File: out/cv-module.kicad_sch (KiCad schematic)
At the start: 189 parts, among them J1 CH1, J10 CTRL2, J11 CTRL3, J2 CH2, J3 CH3, J4 CH4, J5 CH5, J6 CH6, J7 BOND, J8 PWR, J9 CTRL, K101 DPDT latch, K102 DPDT latch, K201 DPDT latch, K202 DPDT latch, K301 DPDT latch, K302 DPDT latch, K401 DPDT latch, K402 DPDT latch, K501 DPDT latch, K502 DPDT latch, K601 DPDT latch, K602 DPDT latch, U1 OPA1644, U10 SSI2164, U11 74AHC541, U12 MAX6126A25, U2 OPA1644, U3 OPA1644, U4 OPA1644, U5 OPA1644, U6 OPA1644, U7 OPA1644, U8 OPA1644, U9 SSI2164

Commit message: Moved md files to docs and no longer have any depedendencies on code in the sibling mixer project
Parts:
- added unit 4 of U8
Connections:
- net AGND: now also R901.2; no longer R901.1
- net IOUT1: no longer C131.2, R132.1, U5.1
- net IOUT2: no longer C231.2, R232.1, U5.7
- net IOUT3: no longer C331.2, R332.1, U5.8
- net IOUT4: no longer C431.2, R432.1, U5.14
- net IOUT5: no longer C531.2, R532.1, U6.1
- net IOUT6: no longer C631.2, R632.1, U6.7
- net MAGND: now also R901.1, R902.1, U8.12 (+); no longer C131.1, C142.1, C231.1, C242.1, C331.1, C342.1, C431.1, C442.1, C531.1, C542.1, C631.1, C642.1, R131.2, R143.2, R231.2, R243.2, R331.2, R343.2, R431.2, R443.2, R531.2, R543.2, R631.2, R643.2, R801.2, R802.1, R901.2, R902.2, U5.13 (-), U5.2 (-), U5.6 (-), U5.9 (-), U6.2 (-), U6.6 (-), U7.13 (-), U7.2 (-), U7.6 (-), U7.9 (-), U8.2 (-), U8.6 (-), U8.9 (-)
- net MDGND: now also R902.2; no longer K101.A2, K101.B2, K102.A2, K102.B2, K201.A2, K201.B2, K202.A2, K202.B2, K301.A2, K301.B2, K302.A2, K302.B2, K401.A2, K401.B2, K402.A2, K402.B2, K501.A2, K501.B2, K502.A2, K502.B2, K601.A2, K601.B2, K602.A2, K602.B2, R902.1
- net RCJ3: now reaches C302.1, R315.2
- net FEN5: now reaches R501.2, R502.1, U2.2 (-)
- net CVX1: now reaches C141.1, R141.2, R142.1, R143.1, R144.2
- net CVX6: now reaches C641.1, R641.2, R642.1, R643.1, R644.2
- net RCJ2: now reaches C202.1, R215.2
- net CVX3: now reaches C341.1, R341.2, R342.1, R343.1, R344.2
- net CVX4: now reaches C441.1, R441.2, R442.1, R443.1, R444.2
- net RCJ5: now reaches C502.1, R515.2
- net FEN6: now reaches R601.2, R602.1, U2.6 (-)
- net CVX2: now reaches C241.1, R241.2, R242.1, R243.1, R244.2
- net RCJ6: now reaches C602.1, R615.2
- net RCJ4: now reaches C402.1, R415.2
- net FEN2: now reaches R201.2, R202.1, U1.6 (-)
- net RCJ1: now reaches C102.1, R115.2
- net CVX5: now reaches C541.1, R541.2, R542.1, R543.1, R544.2
- net FEN1: now reaches R101.2, R102.1, U1.2 (-)
- net FEN3: now reaches R301.2, R302.1, U1.9 (-)
- net FEN4: now reaches R401.2, R402.1, U1.13 (-)
- net KK101R: no longer names the net of K101.B1
- net KK101S: no longer names the net of K101.A1
- net KK102R: no longer names the net of K102.B1
- net KK102S: no longer names the net of K102.A1
- net KK201R: no longer names the net of K201.B1
- net KK201S: no longer names the net of K201.A1
- net KK202R: no longer names the net of K202.B1
- net KK202S: no longer names the net of K202.A1
- net KK301R: no longer names the net of K301.B1
- net KK301S: no longer names the net of K301.A1
- net KK302R: no longer names the net of K302.B1
- net KK302S: no longer names the net of K302.A1
- net KK401R: no longer names the net of K401.B1
- net KK401S: no longer names the net of K401.A1
- net KK402R: no longer names the net of K402.B1
- net KK402S: no longer names the net of K402.A1
- net KK501R: no longer names the net of K501.B1
- net KK501S: no longer names the net of K501.A1
- net KK502R: no longer names the net of K502.B1
- net KK502S: no longer names the net of K502.A1
- net KK601R: no longer names the net of K601.B1
- net KK601S: no longer names the net of K601.A1
- net KK602R: no longer names the net of K602.B1
- net KK602S: no longer names the net of K602.A1
- new net CVN1: C142.1, R143.2, U7.2 (-)
- new net CVN2: C242.1, R243.2, U7.6 (-)
- new net CVN3: C342.1, R343.2, U7.9 (-)
- new net CVN4: C442.1, R443.2, U7.13 (-)
- new net CVN5: C542.1, R543.2, U8.2 (-)
- new net CVN6: C642.1, R643.2, U8.6 (-)
- new net RINV: R801.2, R802.1, U8.9 (-)
- new net SPARE: U8.13 (-), U8.14
- new net SRV1: C131.2, R132.1, U5.1
- new net SRV2: C231.2, R232.1, U5.7
- new net SRV3: C331.2, R332.1, U5.8
- new net SRV4: C431.2, R432.1, U5.14
- new net SRV5: C531.2, R532.1, U6.1
- new net SRV6: C631.2, R632.1, U6.7
- new net SVN1: C131.1, R131.2, U5.2 (-)
- new net SVN2: C231.1, R231.2, U5.6 (-)
- new net SVN3: C331.1, R331.2, U5.9 (-)
- new net SVN4: C431.1, R431.2, U5.13 (-)
- new net SVN5: C531.1, R531.2, U6.2 (-)
- new net SVN6: C631.1, R631.2, U6.6 (-)
- no-connect marks 24 -> 74
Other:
- moved on the sheet: R132, R232, R332, R432, R532, R632, R801, R901, R902

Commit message: tidy up
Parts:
- removed C804: 10u/16V X7R, Capacitor_SMD:C_1210_3225Metric, symbol Device:C

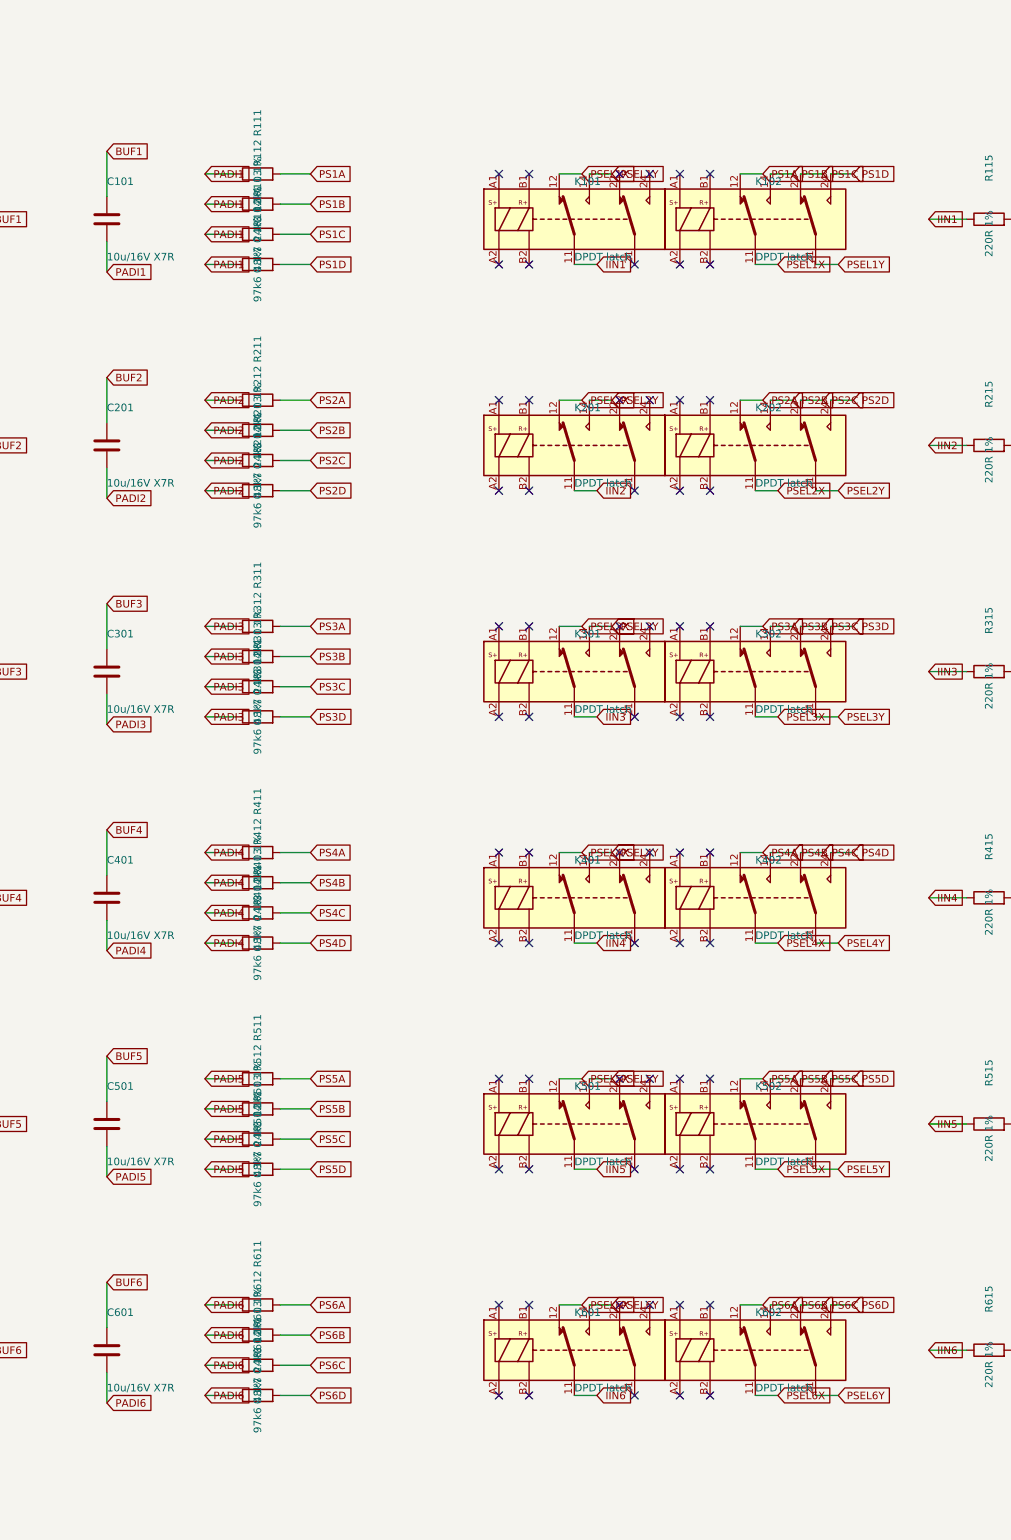
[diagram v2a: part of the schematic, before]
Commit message: TASK — is the 2-bit coarse pad worth 52% of the board?
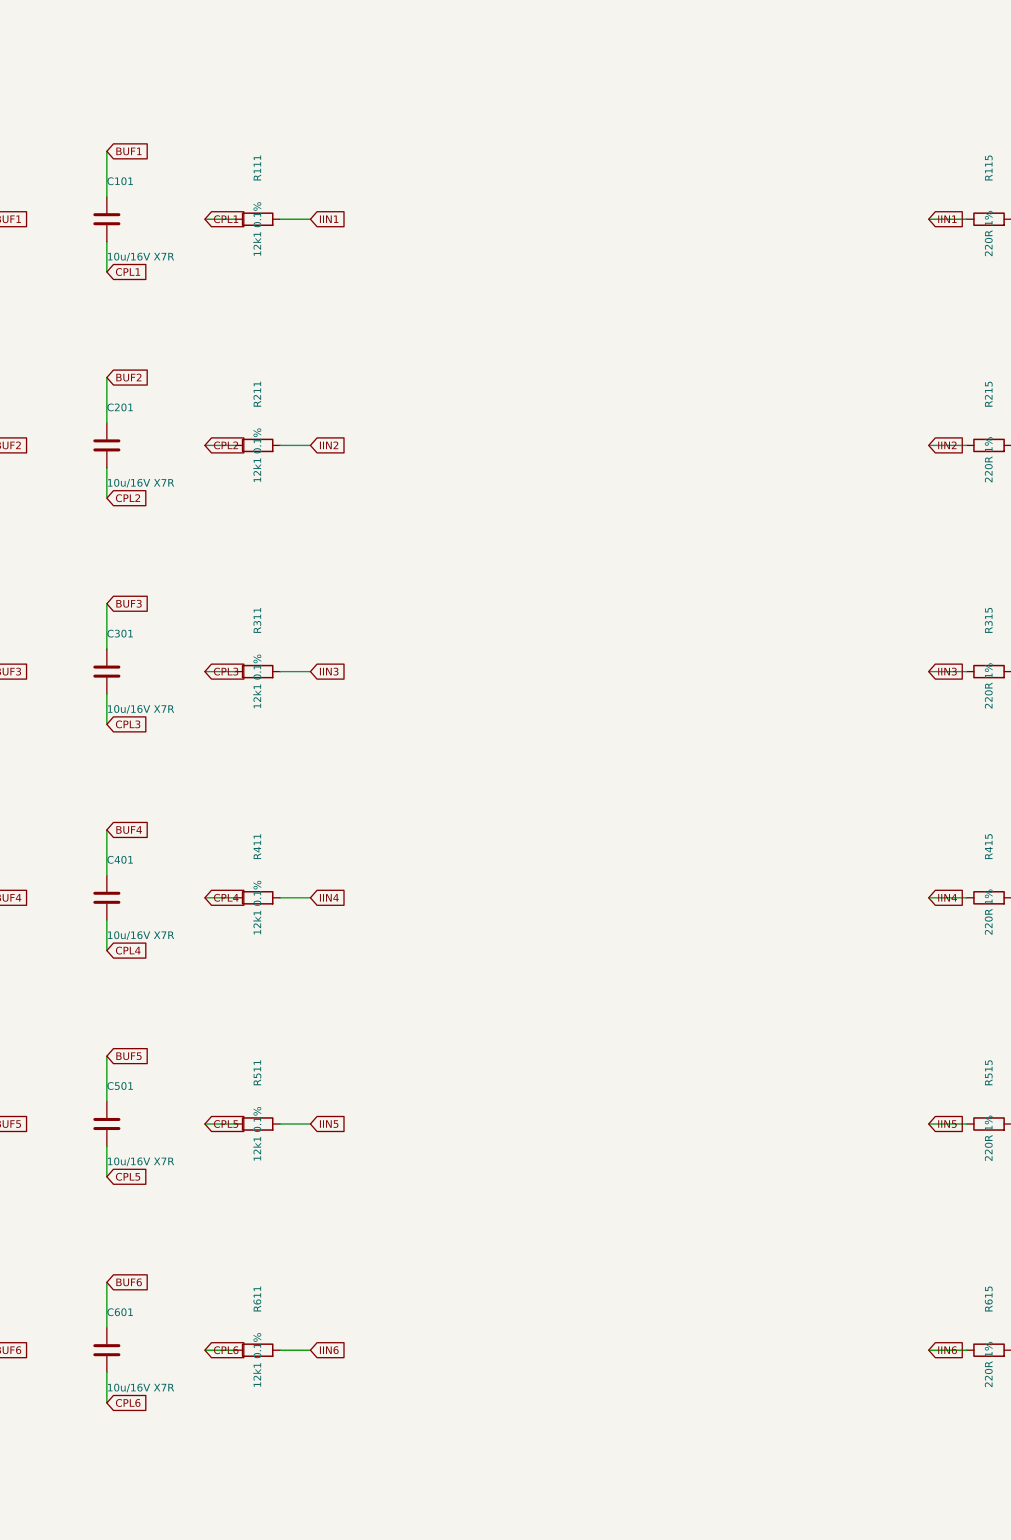
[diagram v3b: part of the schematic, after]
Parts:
- removed K101, K102, K201, K202, K301, K302, K401, K402, K501, K502, K601, K602: DPDT latch, symbol cv:Relay
- removed R112, R212, R312, R412, R512, R612: 24k3 0.1%, Resistor_SMD:R_0805_2012Metric, symbol Device:R
- removed R113, R213, R313, R413, R513, R613: 48k7 0.1%, Resistor_SMD:R_0805_2012Metric, symbol Device:R
- removed R114, R214, R314, R414, R514, R614: 97k6 0.1%, Resistor_SMD:R_0805_2012Metric, symbol Device:R
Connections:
- net PS1A is gone; now on net IIN1: R111.2
- net PS2A is gone; now on net IIN2: R211.2
- net PS3A is gone; now on net IIN3: R311.2
- net PS4A is gone; now on net IIN4: R411.2
- net PS5A is gone; now on net IIN5: R511.2
- net PS6A is gone; now on net IIN6: R611.2
- net PADI1 renamed CPL1
- net PADI2 renamed CPL2
- net PADI3 renamed CPL3
- net PADI4 renamed CPL4
- net PADI5 renamed CPL5
- net PADI6 renamed CPL6
- no-connect marks 74 -> 8
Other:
- moved on the sheet: R111, R211, R311, R411, R511, R611

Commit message: envelope rectifier and fail-safe
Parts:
- added C151, C251, C351, C451, C551, C651: 470n/50V X7R, Capacitor_SMD:C_0805_2012Metric, symbol Device:C
- added C721, C722, C723, C724: 100n/50V X7R, Capacitor_SMD:C_0805_2012Metric, symbol Device:C
- added C805: 2n2/50V C0G, Capacitor_SMD:C_0805_2012Metric, symbol Device:C
- added C806: 1u/16V X7R, Capacitor_SMD:C_0805_2012Metric, symbol Device:C
- added D151, D152, D251, D252, D351, D352, D451, D452, D551, D552, D651, D652: 1N4148W, Diode_SMD:D_SOD-123, symbol Device:D
- added D801, D802, D803, D813, D823, D833: BAT54, Diode_SMD:D_SOD-123, symbol Device:D
- added K801, K802, K803: DPDT, symbol cv:Relay
- added Q801: None, Package_TO_SOT_SMD:SOT-23, symbol cv:Q_NMOS_GSD
- added R151, R152, R153, R155, R251, R252, R253, R255, R351, R352, R353, R355, R451, R452, R453, R455, R551, R552, R553, R555, R651, R652, R653, R655: 10k 1%, Resistor_SMD:R_0805_2012Metric, symbol Device:R
- added R154, R254, R354, R454, R554, R654: 4k99 1%, Resistor_SMD:R_0805_2012Metric, symbol Device:R
- added R803: 100k 1%, Resistor_SMD:R_0805_2012Metric, symbol Device:R
- added U13, U14: TL074, Package_SO:SOIC-14_3.9x8.7mm_P1.27mm, symbol cv:TL074
- added unit 4 of U2
- added unit 3 of U2
- added unit 4 of U4
- added unit 3 of U4
- added unit 4 of U6
- added unit 3 of U6
- J11: footprint Connector_PinHeader_2.54mm:PinHeader_1x03_P2.54mm_Vertical -> Connector_PinHeader_2.54mm:PinHeader_1x05_P2.54mm_Vertical; symbol Connector_Generic:Conn_01x03 -> Connector_Generic:Conn_01x05
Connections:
- net BUF1: now also R151.1, R153.1
- net BUF2: now also R251.1, R253.1
- net BUF3: now also R351.1, R353.1
- net BUF4: now also R451.1, R453.1
- net BUF5: now also R551.1, R553.1
- net BUF6: now also R651.1, R653.1
- net MAGND: now also C721.2, C722.2, C723.2, C724.2, D803.1 (K), U13.10 (+), U13.12 (+), U13.3 (+), U13.5 (+), U14.10 (+), U14.12 (+), U14.3 (+), U14.5 (+), U2.10 (+), U2.12 (+), U4.10 (+), U4.12 (+), U6.10 (+), U6.12 (+)
- net MDGND: now also J11.4 (Pin_4), C806.2, D801.2 (A), Q801.2 (S), R803.2
- net PIN1: now also K801.12
- net PIN2: now also K801.22
- net PIN3: now also K802.12
- net PIN4: now also K802.22
- net PIN5: now also K803.12
- net PIN6: now also K803.22
- net SIN1: now also K801.11; no longer C121.2, R121.2, R131.1, U3.1
- net SIN2: now also K801.21; no longer C221.2, R221.2, R231.1, U3.7
- net SIN3: now also K802.11; no longer C321.2, R321.2, R331.1, U3.8
- net SIN4: now also K802.21; no longer C421.2, R421.2, R431.1, U3.14
- net SIN5: now also K803.11; no longer C521.2, R521.2, R531.1, U4.1
- net SIN6: now also K803.21; no longer C621.2, R621.2, R631.1, U4.7
- net V5: now also D813.1 (K), D823.1 (K), D833.1 (K), K801.A1, K802.A1, K803.A1
- net VA+: now also C721.1, C723.1, U13.4 (V+), U14.4 (V+)
- net VA-: now also C722.1, C724.1, U13.11 (V-), U14.11 (V-)
- net VREFN: now also D803.2 (A)
- net SPARE renamed SPARE0
- new net AOUT1: D151.2 (A), D152.1 (K), U13.1
- new net AOUT2: D251.2 (A), D252.1 (K), U13.7
- new net AOUT3: D351.2 (A), D352.1 (K), U13.8
- new net AOUT4: D451.2 (A), D452.1 (K), U13.14
- new net AOUT5: D551.2 (A), D552.1 (K), U14.1
- new net AOUT6: D651.2 (A), D652.1 (K), U14.7
- new net ENV1: C151.2, R155.2, U2.8
- new net ENV2: C251.2, R255.2, U2.14
- new net ENV3: C351.2, R355.2, U4.8
- new net ENV4: C451.2, R455.2, U4.14
- new net ENV5: C551.2, R555.2, U6.8
- new net ENV6: C651.2, R655.2, U6.14
- new net ENVN1: C151.1, R153.2, R154.2, R155.1, U2.9 (-)
- new net ENVN2: C251.1, R253.2, R254.2, R255.1, U2.13 (-)
- new net ENVN3: C351.1, R353.2, R354.2, R355.1, U4.9 (-)
- new net ENVN4: C451.1, R453.2, R454.2, R455.1, U4.13 (-)
- new net ENVN5: C551.1, R553.2, R554.2, R555.1, U6.9 (-)
- new net ENVN6: C651.1, R653.2, R654.2, R655.1, U6.13 (-)
- new net FSAC: C805.2, D801.1 (K), D802.2 (A)
- new net FSD: D813.2 (A), D823.2 (A), D833.2 (A), K801.A2, K802.A2, K803.A2, Q801.3 (D)
- new net FSDRV: C805.1, J11.5 (Pin_5)
- new net FSG: C806.1, D802.1 (K), Q801.1 (G), R803.1
- new net HW1: D152.2 (A), R152.2, R154.1
- new net HW2: D252.2 (A), R252.2, R254.1
- new net HW3: D352.2 (A), R352.2, R354.1
- new net HW4: D452.2 (A), R452.2, R454.1
- new net HW5: D552.2 (A), R552.2, R554.1
- new net HW6: D652.2 (A), R652.2, R654.1
- new net HWN1: D151.1 (K), R151.2, R152.1, U13.2 (-)
- new net HWN2: D251.1 (K), R251.2, R252.1, U13.6 (-)
- new net HWN3: D351.1 (K), R351.2, R352.1, U13.9 (-)
- new net HWN4: D451.1 (K), R451.2, R452.1, U13.13 (-)
- new net HWN5: D551.1 (K), R551.2, R552.1, U14.2 (-)
- new net HWN6: D651.1 (K), R651.2, R652.1, U14.6 (-)
- new net IVOUT1: C121.2, K801.14, R121.2, R131.1, U3.1
- new net IVOUT2: C221.2, K801.24, R221.2, R231.1, U3.7
- new net IVOUT3: C321.2, K802.14, R321.2, R331.1, U3.8
- new net IVOUT4: C421.2, K802.24, R421.2, R431.1, U3.14
- new net IVOUT5: C521.2, K803.14, R521.2, R531.1, U4.1
- new net IVOUT6: C621.2, K803.24, R621.2, R631.1, U4.7
- new net SPARE1: U14.8, U14.9 (-)
- new net SPARE2: U14.13 (-), U14.14
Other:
- note added: "Fail-safe: any stuck MCU state collapses the pump, the FET releases, and de-energised is bypass. D803 covers the one path the pump cannot see. See design.fail_safe()."
- moved on the sheet: C701, C702, C703, C704, C705, C706, C707, C708, C709, C710, C711, C712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

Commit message: Next increment
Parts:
- D803: value BAT54 -> PMEG2010AEH; footprint Diode_SMD:D_SOD-123 -> Diode_SMD:D_SOD-123F
- Q801: value None -> DMG1012T; footprint Package_TO_SOT_SMD:SOT-23 -> Package_TO_SOT_SMD:SOT-523
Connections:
- net FSD: now also K801.12, K802.12, K803.12; no longer K801.A2, K802.A2, K803.A2
- net IVOUT1: now also K801.8; no longer K801.14
- net IVOUT2: now also K801.5; no longer K801.24
- net IVOUT3: now also K802.8; no longer K802.14
- net IVOUT4: now also K802.5; no longer K802.24
- net IVOUT5: now also K803.8; no longer K803.14
- net IVOUT6: now also K803.5; no longer K803.24
- net PIN1: now also K801.10; no longer K801.12
- net PIN2: now also K801.3; no longer K801.22
- net PIN3: now also K802.10; no longer K802.12
- net PIN4: now also K802.3; no longer K802.22
- net PIN5: now also K803.10; no longer K803.12
- net PIN6: now also K803.3; no longer K803.22
- net SIN1: now also K801.9; no longer K801.11
- net SIN2: now also K801.4; no longer K801.21
- net SIN3: now also K802.9; no longer K802.11
- net SIN4: now also K802.4; no longer K802.21
- net SIN5: now also K803.9; no longer K803.11
- net SIN6: now also K803.4; no longer K803.21
- net V5: now also K801.1, K802.1, K803.1; no longer K801.A1, K802.A1, K803.A1
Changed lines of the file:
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@@
 		(pts
 			(xy 815.34 977.9)
-			(xy 815.34 965.2)
+			(xy 815.34 970.28)
 		)
 		(stroke
@@
 		(pts
 			(xy 820.42 977.9)
-			(xy 820.42 960.12)
+			(xy 820.42 970.28)
 		)
 		(stroke
@@
 		(pts
 			(xy 825.5 977.9)
-			(xy 825.5 955.04)
+			(xy 825.5 970.28)
 		)
 		(stroke
@@
 		(pts
 			(xy 866.14 977.9)
-			(xy 866.14 965.2)
+			(xy 866.14 970.28)
 		)
 		(stroke
@@
 		(pts
 			(xy 871.22 977.9)
-			(xy 871.22 960.12)
+			(xy 871.22 970.28)
 		)
 		(stroke
@@
 		(pts
 			(xy 876.3 977.9)
-			(xy 876.3 955.04)
+			(xy 876.3 970.28)
 		)
 		(stroke
@@
 		(pts
 			(xy 916.94 977.9)
-			(xy 916.94 965.2)
+			(xy 916.94 970.28)
 		)
 		(stroke
@@
 		(pts
 			(xy 922.02 977.9)
-			(xy 922.02 960.12)
+			(xy 922.02 970.28)
 		)
 		(stroke
@@
 		(pts
 			(xy 927.1 977.9)
-			(xy 927.1 955.04)
+			(xy 927.1 970.28)
 		)
 		(stroke
@@
 	(global_label "IVOUT1"
 		(shape input)
-		(at 815.34 965.2 0)
+		(at 815.34 970.28 0)
 		(effects
 			(font
@@
 	(global_label "PIN2"
 		(shape input)
-		(at 820.42 960.12 0)
+		(at 820.42 970.28 0)
 		(effects
 			(font
@@
 	(global_label "IVOUT2"
 		(shape input)
-		(at 825.5 955.04 0)
+		(at 825.5 970.28 0)
 		(effects
 			(font
@@
 	(global_label "IVOUT3"
 		(shape input)
-		(at 866.14 965.2 0)
+		(at 866.14 970.28 0)
 		(effects
 			(font
@@
 	(global_label "PIN4"
 		(shape input)
-		(at 871.22 960.12 0)
+		(at 871.22 970.28 0)
 		(effects
 			(font
@@
 	(global_label "IVOUT4"
 		(shape input)
-		(at 876.3 955.04 0)
+		(at 876.3 970.28 0)
 		(effects
 			(font
@@
 	(global_label "IVOUT5"
 		(shape input)
-		(at 916.94 965.2 0)
+		(at 916.94 970.28 0)
 		(effects
 			(font
@@
 	(global_label "PIN6"
 		(shape input)
-		(at 922.02 960.12 0)
+		(at 922.02 970.28 0)
 		(effects
 			(font
@@
 	(global_label "IVOUT6"
 		(shape input)
-		(at 927.1 955.04 0)
+		(at 927.1 970.28 0)
 		(effects
 			(font
@@
 			)
 		)
-		(property "Value" "None"
+		(property "Value" "DMG1012T"
 			(at 1016 946.15 0)
 			(effects
@@
 			)
 		)
-		(property "Footprint" "Package_TO_SOT_SMD:SOT-23"
+		(property "Footprint" "Package_TO_SOT_SMD:SOT-523"
 			(at 1016 939.8 0)
 			(effects
@@
 			)
 		)
-		(pin "11"
+		(pin "1"
 		)
-		(pin "12"
+		(pin "3"
 		)
-		(pin "14"
+		(pin "4"
 		)
-		(pin "21"
+		(pin "5"
 		)
-		(pin "22"
+		(pin "8"
 		)
-		(pin "24"
+		(pin "9"
 		)
-		(pin "A1"
+		(pin "10"
 		)
-		(pin "A2"
+		(pin "12"
 		)
 		(instances
@@
 			)
 		)
-		(pin "11"
+		(pin "1"
 		)
-		(pin "12"
+		(pin "3"
 		)
-		(pin "14"
+		(pin "4"
 		)
-		(pin "21"
+		(pin "5"
 		)
-		(pin "22"
+		(pin "8"
 		)
-		(pin "24"
+		(pin "9"
 		)
-		(pin "A1"
+		(pin "10"
 		)
-		(pin "A2"
+		(pin "12"
 		)
 		(instances
@@
 			)
 		)
-		(pin "11"
+		(pin "1"
 		)
-		(pin "12"
+		(pin "3"
 		)
-		(pin "14"
+		(pin "4"
 		)
-		(pin "21"
+		(pin "5"
 		)
-		(pin "22"
+		(pin "8"
 		)
-		(pin "24"
+		(pin "9"
 		)
-		(pin "A1"
+		(pin "10"
 		)
-		(pin "A2"
+		(pin "12"
 		)
 		(instances
@@
 			)
 		)
-		(property "Value" "BAT54"
+		(property "Value" "PMEG2010AEH"
 			(at 1092.2 946.15 0)
 			(effects
@@
 			)
 		)
-		(property "Footprint" "Diode_SMD:D_SOD-123"
+		(property "Footprint" "Diode_SMD:D_SOD-123F"
 			(at 1092.2 939.8 0)
 			(effects

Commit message: DC_DC power
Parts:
- added C807, C808, C811, C812, C813: 10u/50V X7R, Capacitor_SMD:C_1210_3225Metric, symbol Device:C
- added C809: 100n/50V X7R, Capacitor_SMD:C_0805_2012Metric, symbol Device:C
- added C810: 470n/50V X7R, Capacitor_SMD:C_0805_2012Metric, symbol Device:C
- added C814: 10u/16V X7R, Capacitor_SMD:C_1210_3225Metric, symbol Device:C
- added D804: B340A, Diode_SMD:D_SMA, symbol Device:D_Schottky
- added R804, R805: 4R7 1%, Resistor_SMD:R_0805_2012Metric, symbol Device:R
- added U15: TMR6-2422WI, cv:TRACO_TMR-6-xxxxWI_Dual_THT, symbol cv:TMR6-2422WI
- added U16: NCP1117-5.0, Package_TO_SOT_SMD:TO-252-2, symbol cv:NCP1117-5.0
- J8: footprint Connector_PinHeader_2.54mm:PinHeader_1x05_P2.54mm_Vertical -> Connector_PinHeader_2.54mm:PinHeader_1x02_P2.54mm_Vertical; symbol Connector_Generic:Conn_01x05 -> Connector_Generic:Conn_01x02
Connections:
- net MAGND: no longer J8.3 (Pin_3)
- net MDGND: now also C810.2, C811.2, C812.2, C813.2, C814.2, U15.7 (Com), U16.1 (GND); no longer J8.5 (Pin_5)
- net V5: now also C814.1, U16.2 (VO); no longer J8.4 (Pin_4)
- net VA+: now also C811.1, R804.2; no longer J8.1 (Pin_1)
- net VA-: now also C812.1, R805.2; no longer J8.2 (Pin_2)
- new net IGND: C807.2, C808.2, C809.2, C810.1, J8.2 (Pin_2), U15.1 (-Vin), U15.3 (Remote)
- new net VA_RAW: C813.1, R804.1, U15.6 (+Vout), U16.3 (VI)
- new net VIN: D804.2 (A), J8.1 (Pin_1)
- new net VIN_P: C807.1, C808.1, C809.1, D804.1 (K), U15.2 (+Vin)
- new net VN_RAW: R805.1, U15.8 (-Vout)
- no-connect marks 8 -> 9
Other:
- note added: "The isolation barrier runs through U15: pins 1-3 are referenced to IGND, which is the inlet's 0 V and the mixer's PGND through the shared jack; pins 6-8 to MDGND. C810 is the only other part that touches both. See design.barrier_return()."
